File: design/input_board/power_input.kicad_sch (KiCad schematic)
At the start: 20 parts, among them J4 BATT In, Q1 CSD19537Q3, Q2 BSS138, SW1 SW_SPST_LED, U1 TPS26631PWP

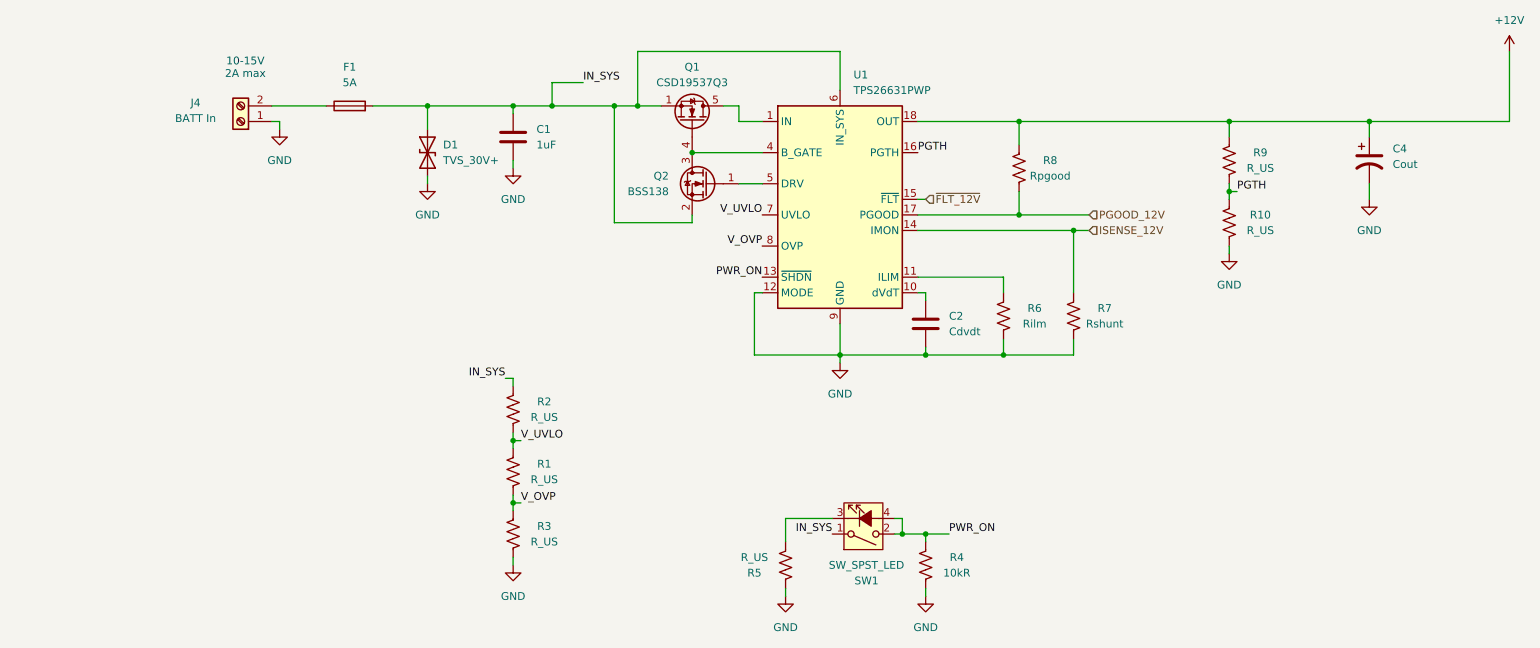
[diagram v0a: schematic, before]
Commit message: Finihs schamtic and footprints; DVDD 3.3->2V
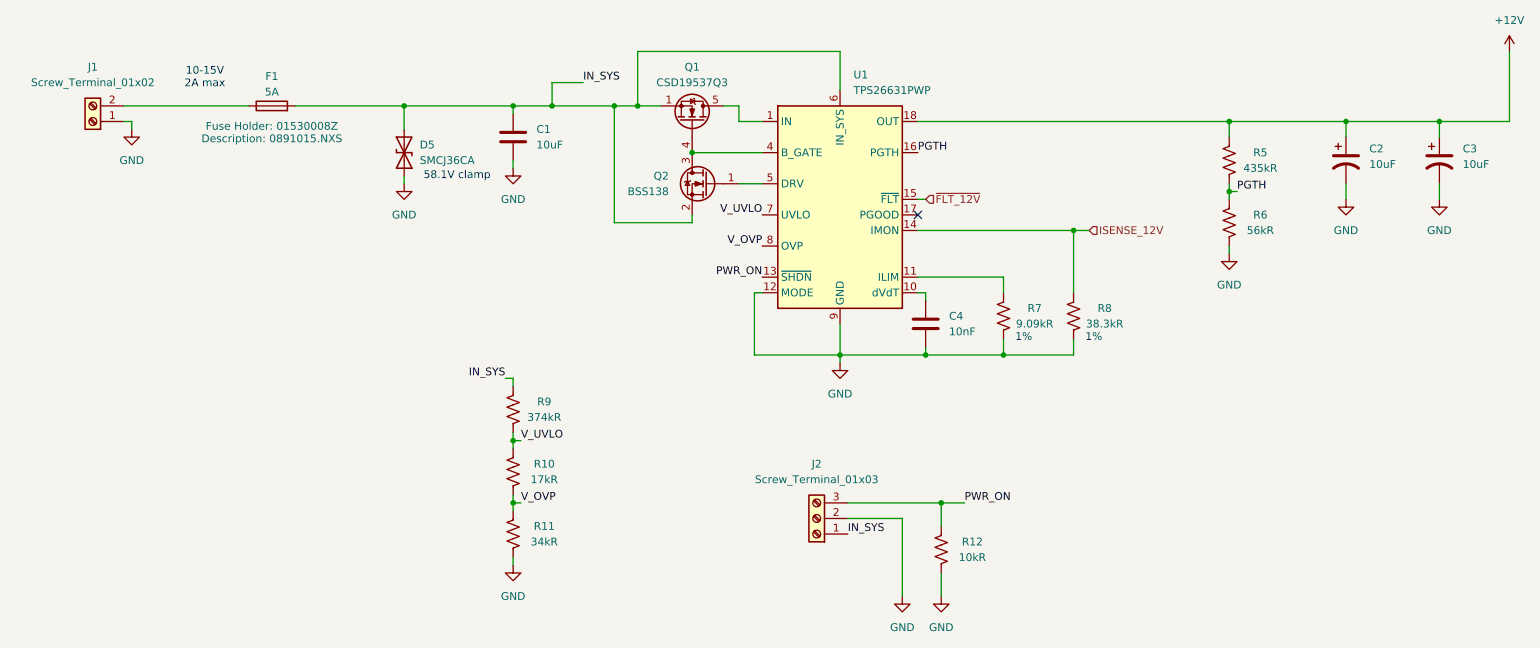
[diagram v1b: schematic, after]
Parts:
- removed J4: BATT In, symbol Connector:Screw_Terminal_01x02
- removed R5: R_US, symbol Device:R_US
- removed R8: Rpgood, symbol Device:R_US
- removed SW1: SW_SPST_LED, symbol Switch:SW_SPST_LED
- added C3: 10uF, Capacitor_SMD:C_0805_2012Metric_Pad1.18x1.45mm_HandSolder, symbol Device:C_Polarized_US
- added J1: Screw_Terminal_01x02, TerminalBlock_Phoenix:TerminalBlock_Phoenix_MKDS-1,5-2-5.08_1x02_P5.08mm_Horizontal, symbol Connector:Screw_Terminal_01x02
- added J2: Screw_Terminal_01x03, TerminalBlock_Phoenix:TerminalBlock_Phoenix_MKDS-1,5-3-5.08_1x03_P5.08mm_Horizontal, symbol Connector:Screw_Terminal_01x03
- C1: value 1uF -> 10uF; footprint (none) -> Capacitor_SMD:C_0805_2012Metric_Pad1.18x1.45mm_HandSolder
- C2: renamed from C4; value Cout -> 10uF; footprint (none) -> Capacitor_SMD:C_0805_2012Metric_Pad1.18x1.45mm_HandSolder
- C4: renamed from C2; value Cdvdt -> 10nF; footprint (none) -> Capacitor_SMD:C_0805_2012Metric_Pad1.18x1.45mm_HandSolder
- D5: renamed from D1; value TVS_30V+ -> SMCJ36CA; footprint Diode_SMD:D_SMC -> Diode_SMD:D_SMC_Handsoldering
- F1: footprint (none) -> input_board:01530009Z; Fuse Holder (none) -> 01530008Z
- R10: renamed from R1; value R_US -> 17kR; footprint (none) -> Resistor_SMD:R_0805_2012Metric_Pad1.20x1.40mm_HandSolder
- R11: renamed from R3; value R_US -> 34kR; footprint (none) -> Resistor_SMD:R_0805_2012Metric_Pad1.20x1.40mm_HandSolder
- R12: renamed from R4; footprint (none) -> Resistor_SMD:R_0805_2012Metric_Pad1.20x1.40mm_HandSolder
- R5: renamed from R9; value R_US -> 435kR; footprint (none) -> Resistor_SMD:R_0805_2012Metric_Pad1.20x1.40mm_HandSolder
- R6: renamed from R10; value R_US -> 56kR; footprint (none) -> Resistor_SMD:R_0805_2012Metric_Pad1.20x1.40mm_HandSolder
- R7: renamed from R6; value Rilm -> 9.09kR; footprint (none) -> Resistor_SMD:R_0805_2012Metric_Pad1.20x1.40mm_HandSolder
- R8: renamed from R7; value Rshunt -> 38.3kR; footprint (none) -> Resistor_SMD:R_0805_2012Metric_Pad1.20x1.40mm_HandSolder
- R9: renamed from R2; value R_US -> 374kR; footprint (none) -> Resistor_SMD:R_0805_2012Metric_Pad1.20x1.40mm_HandSolder
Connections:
- net +12V: now also C3.1
- net GND: now also C3.2, J1.1 (Pin_1), J2.2 (Pin_2)
- net IN_SYS: now also J2.1 (Pin_1)
- net PWR_ON: now also J2.3 (Pin_3)
- net at F1.1: now also J1.2 (Pin_2)
- net PGOOD_12V: no longer names the net of U1.17 (PGOOD)
- no-connect marks 0 -> 1
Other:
- note added: "1%"
- note added: "58.1V clamp"
- moved on the sheet: C2, D5, R12

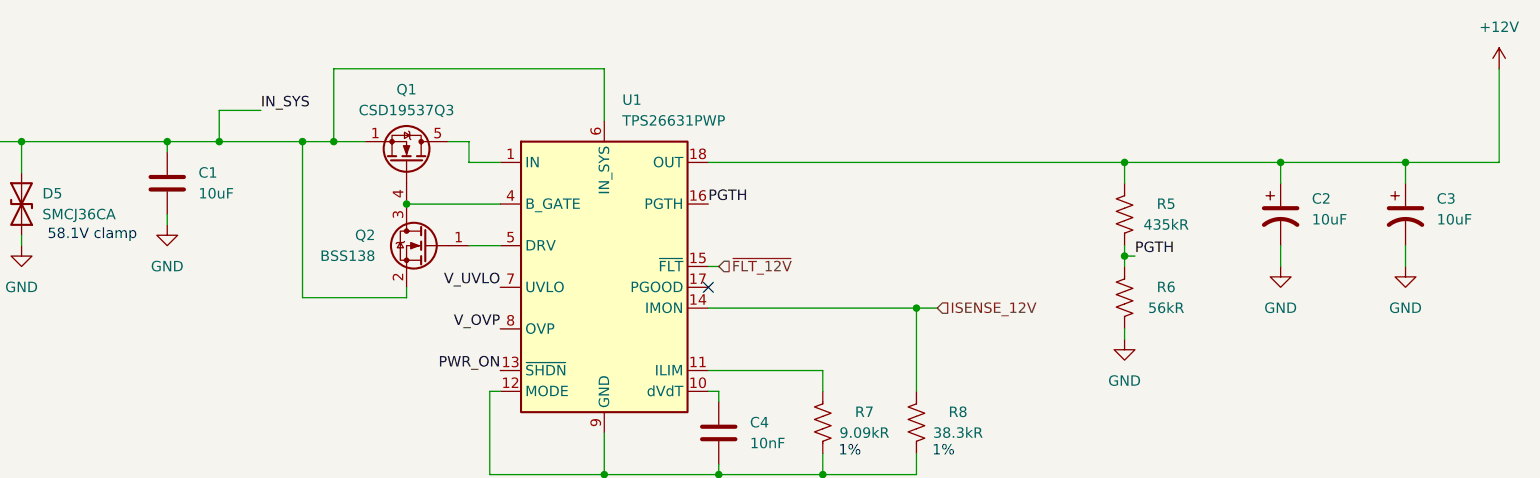
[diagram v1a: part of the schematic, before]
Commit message: Layout v1, its bad
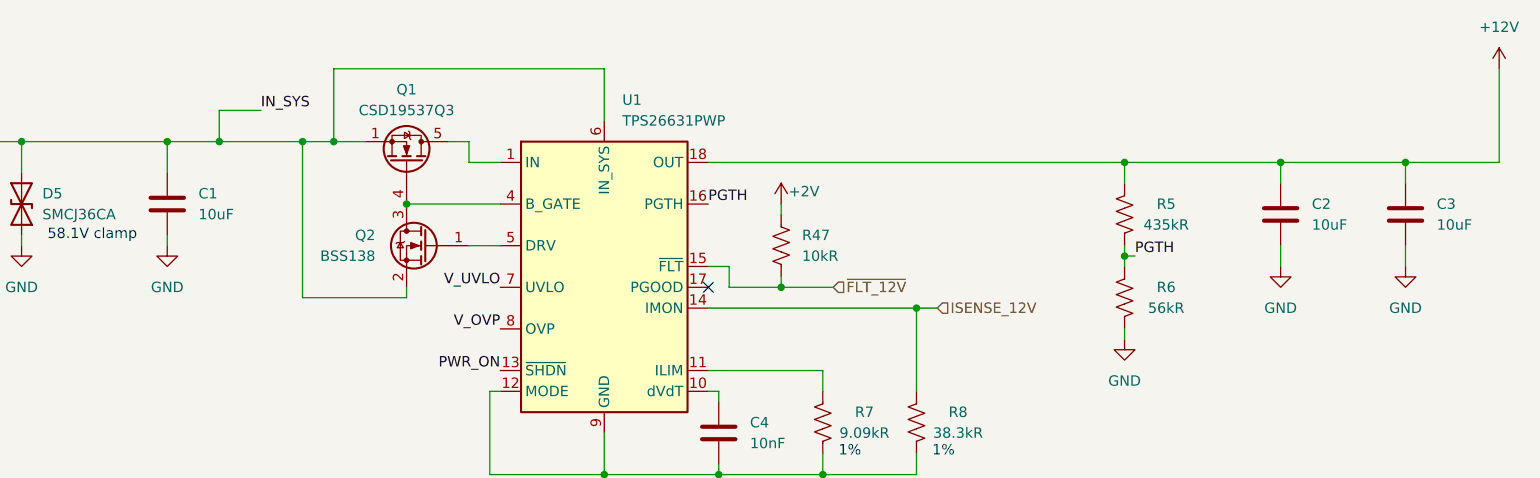
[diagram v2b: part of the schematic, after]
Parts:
- added R47: 10kR, Resistor_SMD:R_0805_2012Metric_Pad1.20x1.40mm_HandSolder, symbol Device:R_US
- C2, C3: symbol Device:C_Polarized_US -> Device:C
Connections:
- net ~{FLT_12V}: now also R47.2
- new net +2V: R47.1
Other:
- moved on the sheet: C1
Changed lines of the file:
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@@
+	)
+	(junction
+		(at 172.72 83.82)
+		(diameter 0)
+		(color 0 0 0 0)
 	)
 	(junction
@@
 	(wire
 		(pts
-			(xy 97.79 74.93) (xy 97.79 76.2)
+			(xy 97.79 77.47) (xy 97.79 78.74)
 		)
 		(stroke
@@
 	(wire
 		(pts
+			(xy 166.37 83.82) (xy 166.37 81.28)
+		)
+		(stroke
+			(width 0)
+			(type default)
+		)
+	)
+	(wire
+		(pts
 			(xy 152.4 133.35) (xy 161.29 133.35)
 		)
@@
 	(wire
 		(pts
+			(xy 172.72 82.55) (xy 172.72 83.82)
+		)
+		(stroke
+			(width 0)
+			(type default)
+		)
+	)
+	(wire
+		(pts
+			(xy 172.72 83.82) (xy 166.37 83.82)
+		)
+		(stroke
+			(width 0)
+			(type default)
+		)
+	)
+	(wire
+		(pts
 			(xy 134.62 68.58) (xy 138.43 68.58)
 		)
@@
 	(wire
 		(pts
+			(xy 172.72 74.93) (xy 172.72 73.66)
+		)
+		(stroke
+			(width 0)
+			(type default)
+		)
+	)
+	(wire
+		(pts
 			(xy 167.64 130.81) (xy 171.45 130.81)
 		)
@@
 	(wire
 		(pts
-			(xy 165.1 81.28) (xy 163.83 81.28)
-		)
-		(stroke
-			(width 0)
-			(type default)
-		)
-	)
-	(wire
-		(pts
 			(xy 97.79 130.81) (xy 99.06 130.81)
 		)
@@
 	(wire
 		(pts
+			(xy 166.37 81.28) (xy 163.83 81.28)
+		)
+		(stroke
+			(width 0)
+			(type default)
+		)
+	)
+	(wire
+		(pts
 			(xy 151.13 106.68) (xy 151.13 107.95)
 		)
@@
 	(wire
 		(pts
-			(xy 97.79 67.31) (xy 97.79 66.04)
+			(xy 97.79 69.85) (xy 97.79 66.04)
 		)
 		(stroke
@@
 		(pts
 			(xy 151.13 57.15) (xy 118.11 57.15)
+		)
+		(stroke
+			(width 0)
+			(type default)
+		)
+	)
+	(wire
+		(pts
+			(xy 172.72 83.82) (xy 179.07 83.82)
 		)
 		(stroke
@@
 	(hierarchical_label "~{FLT_12V}"
 		(shape input)
-		(at 165.1 81.28 0)
+		(at 179.07 83.82 0)
 		(effects
 			(font
@@
 	(symbol
 		(lib_id "Device:C")
-		(at 97.79 71.12 0)
+		(at 97.79 73.66 0)
 		(unit 1)
 		(exclude_from_sim no)
@@
 		(fields_autoplaced yes)
 		(property "Reference" "C1"
-			(at 101.6 69.8499 0)
+			(at 101.6 72.3899 0)
 			(effects
 				(font
@@
 		)
 		(property "Value" "10uF"
-			(at 101.6 72.3899 0)
+			(at 101.6 74.9299 0)
 			(effects
 				(font
@@
 		)
 		(property "Footprint" "Capacitor_SMD:C_0805_2012Metric_Pad1.18x1.45mm_HandSolder"
-			(at 98.7552 74.93 0)
+			(at 98.7552 77.47 0)
 			(effects
 				(font
@@
 		)
 		(property "Datasheet" "~"
-			(at 97.79 71.12 0)
+			(at 97.79 73.66 0)
 			(effects
 				(font
@@
 		)
 		(property "Description" "Unpolarized capacitor"
-			(at 97.79 71.12 0)
+			(at 97.79 73.66 0)
 			(effects
 				(font
@@
 				(path "/edc2dfd5-6e83-475f-94b9-1e03bbedf967/d77752ba-70f1-4433-8fab-aebaef693683"
 					(reference "R11")
+					(unit 1)
+				)
+			)
+		)
+	)
+	(symbol
+		(lib_id "Device:R_US")
+		(at 172.72 78.74 0)
+		(unit 1)
+		(exclude_from_sim no)
+		(in_bom yes)
+		(on_board yes)
+		(dnp no)
+		(fields_autoplaced yes)
+		(property "Reference" "R47"
+			(at 175.26 77.4699 0)
+			(effects
+				(font
+					(size 1.27 1.27)
+				)
+				(justify left)
+			)
+		)
+		(property "Value" "10kR"
+			(at 175.26 80.0099 0)
+			(effects
+				(font
+					(size 1.27 1.27)
+				)
+				(justify left)
+			)
+		)
+		(property "Footprint" "Resistor_SMD:R_0805_2012Metric_Pad1.20x1.40mm_HandSolder"
+			(at 173.736 78.994 90)
+			(effects
+				(font
+					(size 1.27 1.27)
+				)
+				(hide yes)
+			)
+		)
+		(property "Datasheet" "~"
+			(at 172.72 78.74 0)
+			(effects
+				(font
+					(size 1.27 1.27)
+				)
+				(hide yes)
+			)
+		)
+		(property "Description" "Resistor, US symbol"
+			(at 172.72 78.74 0)
+			(effects
+				(font
+					(size 1.27 1.27)
+				)
+				(hide yes)
+			)
+		)
+		(pin "2"
+		)
+		(pin "1"
+		)
+		(instances
+			(project ""
+				(path "/edc2dfd5-6e83-475f-94b9-1e03bbedf967/d77752ba-70f1-4433-8fab-aebaef693683"
+					(reference "R47")
 					(unit 1)
 				)
@@
 	)
 	(symbol
-		(lib_id "Device:C_Polarized_US")
+		(lib_id "Device:C")
 		(at 248.92 74.93 0)
 		(unit 1)
@@
 		(fields_autoplaced yes)
 		(property "Reference" "C3"
-			(at 252.73 73.0249 0)
+			(at 252.73 73.6599 0)
 			(effects
 				(font
@@
 		)
 		(property "Value" "10uF"
-			(at 252.73 75.5649 0)
+			(at 252.73 76.1999 0)
 			(effects
 				(font
@@
 		)
 		(property "Footprint" "Capacitor_SMD:C_0805_2012Metric_Pad1.18x1.45mm_HandSolder"
-			(at 248.92 74.93 0)
+			(at 249.8852 78.74 0)
 			(effects
 				(font
@@
 			)
 		)
-		(property "Description" "Polarized capacitor, US symbol"
+		(property "Description" "Unpolarized capacitor"
 			(at 248.92 74.93 0)
 			(effects
@@
 	(symbol
 		(lib_id "power:GND")
-		(at 97.79 76.2 0)
+		(at 97.79 78.74 0)
 		(unit 1)
 		(exclude_from_sim no)
@@
 		(fields_autoplaced yes)
 		(property "Reference" "#PWR012"
-			(at 97.79 82.55 0)
+			(at 97.79 85.09 0)
 			(effects
 				(font
@@
 		)
 		(property "Value" "GND"
-			(at 97.79 81.28 0)
+			(at 97.79 83.82 0)
 			(effects
 				(font
@@
 		)
 		(property "Footprint" ""
-			(at 97.79 76.2 0)
+			(at 97.79 78.74 0)
 			(effects
 				(font
@@
 		)
 		(property "Datasheet" ""
-			(at 97.79 76.2 0)
+			(at 97.79 78.74 0)
 			(effects
 				(font
@@
 		)
 		(property "Description" "Power symbol creates a global label with name \"GND\" , ground"
-			(at 97.79 76.2 0)
+			(at 97.79 78.74 0)
 			(effects
 				(font
@@
 	)
 	(symbol
-		(lib_id "Device:C_Polarized_US")
+		(lib_id "Device:C")
 		(at 233.68 74.93 0)
 		(unit 1)
@@
 		(fields_autoplaced yes)
 		(property "Reference" "C2"
-			(at 237.49 73.0249 0)
+			(at 237.49 73.6599 0)
 			(effects
 				(font
@@
 		)
 		(property "Value" "10uF"
-			(at 237.49 75.5649 0)
+			(at 237.49 76.1999 0)
 			(effects
 				(font
@@
 		)
 		(property "Footprint" "Capacitor_SMD:C_0805_2012Metric_Pad1.18x1.45mm_HandSolder"
-			(at 233.68 74.93 0)
+			(at 234.6452 78.74 0)
 			(effects
 				(font
@@
 			)
 		)
-		(property "Description" "Polarized capacitor, US symbol"
+		(property "Description" "Unpolarized capacitor"
 			(at 233.68 74.93 0)
 			(effects
@@
 					(unit 1)
 				)
+			)
+		)
+	)
+	(symbol
+		(lib_id "input_board:+2V")
+		(at 172.72 73.66 0)
+		(unit 1)
+		(exclude_from_sim no)
+		(in_bom yes)
+		(on_board yes)
+		(dnp no)
+		(property "Reference" "#PWR0147"
+			(at 172.72 77.47 0)
+			(effects
+				(font
+					(size 1.27 1.27)
+				)
+				(hide yes)
+			)
+		)
+		(property "Value" "+2V"
+			(at 175.514 72.136 0)
+			(effects
+				(font
+					(size 1.27 1.27)
+				)
+			)
+		)
+		(property "Footprint" ""
+			(at 172.72 73.66 0)
+			(effects
+				(font
+					(size 1.27 1.27)
+				)
+				(hide yes)
+			)
+		)
+		(property "Datasheet" ""
+			(at 172.72 73.66 0)
+			(effects
+				(font
+					(size 1.27 1.27)
+				)
+				(hide yes)
+			)
+		)
+		(property "Description" "Power symbol creates a global label with name \"+2V\""
+			(at 172.72 73.66 0)
+			(effects
+				(font
+					(size 1.27 1.27)
+				)
+				(hide yes)
+			)
+		)
+		(pin "1"
+		)
+		(instances
+			(project ""
+				(path "/edc2dfd5-6e83-475f-94b9-1e03bbedf967/d77752ba-70f1-4433-8fab-aebaef693683"
+					(reference "#PWR0147")
+					(unit 1)
+				)

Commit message: Layout v2; better
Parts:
- removed C2, C3: 10uF, Capacitor_SMD:C_0805_2012Metric_Pad1.18x1.45mm_HandSolder, symbol Device:C
- J2: footprint TerminalBlock_Phoenix:TerminalBlock_Phoenix_MKDS-1,5-3-5.08_1x03_P5.08mm_Horizontal -> Connector_PinHeader_2.54mm:PinHeader_1x03_P2.54mm_Vertical
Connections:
- net GND: now also J1.2 (Pin_2); no longer J1.1 (Pin_1)
- net at F1.1: now also J1.1 (Pin_1); no longer J1.2 (Pin_2)
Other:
- moved on the sheet: J1
